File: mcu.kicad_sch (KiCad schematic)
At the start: 41 parts, among them J10 MCU_SWD, J11 JST_06, J12 Bluetooth, J6 MTRBTN, J7 SPI_DBG, J8 BuzzerHV, J9 BuzzerLV, Q3 MMBTA42, U4 STM32F103C8Tx

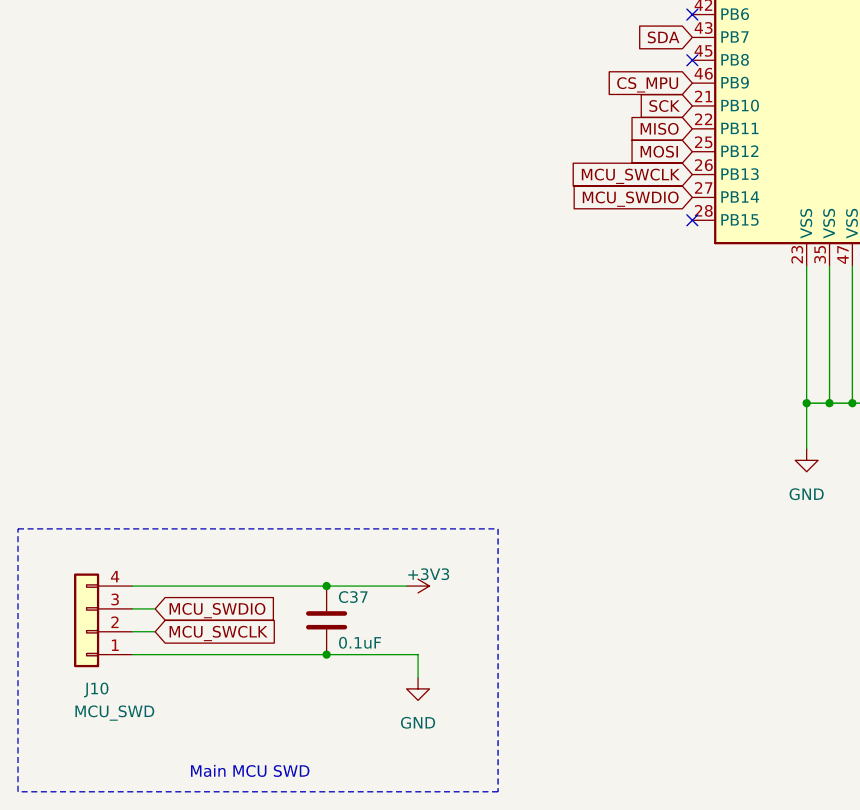
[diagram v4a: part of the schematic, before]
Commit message: removed swd
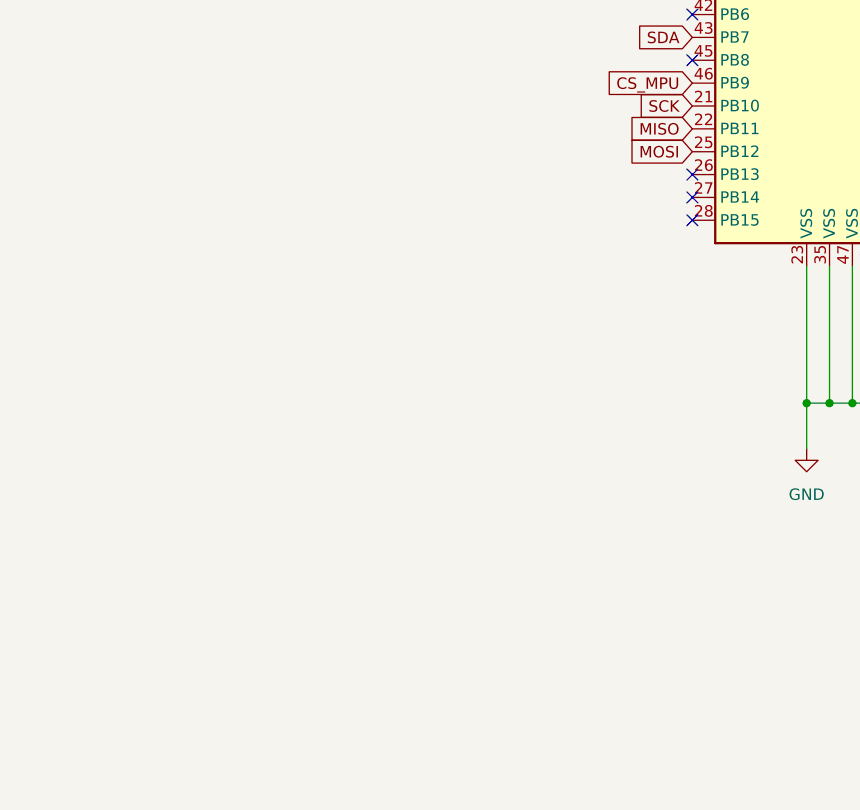
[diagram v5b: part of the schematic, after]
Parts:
- removed C37: 0.1uF, Capacitor_SMD:C_0603_1608Metric_Pad1.08x0.95mm_HandSolder, symbol Device:C
- removed J10: MCU_SWD, Connector_PinSocket_2.54mm:PinSocket_1x04_P2.54mm_Vertical, symbol Connector_Generic:Conn_01x04
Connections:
- net MCU_SWCLK: no longer names the net of U4.26 (PB13)
- net MCU_SWDIO: no longer names the net of U4.27 (PB14)
- no-connect marks 13 -> 15
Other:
- note removed: "Main MCU SWD"
